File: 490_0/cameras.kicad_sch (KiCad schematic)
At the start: 2 parts, among them J1 ArduCAM ToF Camera, J2 ArduCAM ToF Camera

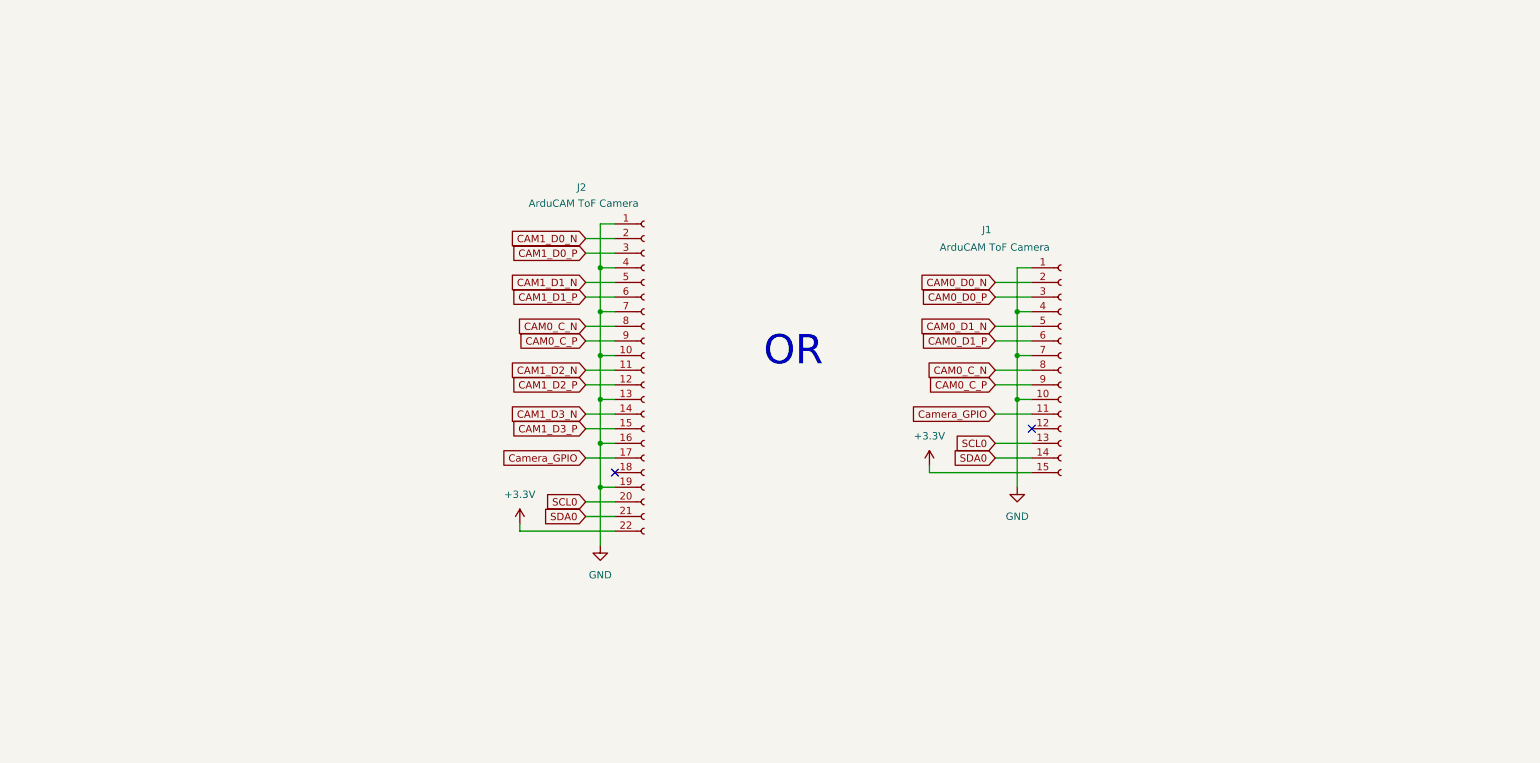
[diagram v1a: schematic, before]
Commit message: Changed the camera connectors
- Added 2 and 4 lane MIPI 22 lane connectors
- Added digikey link to a good type
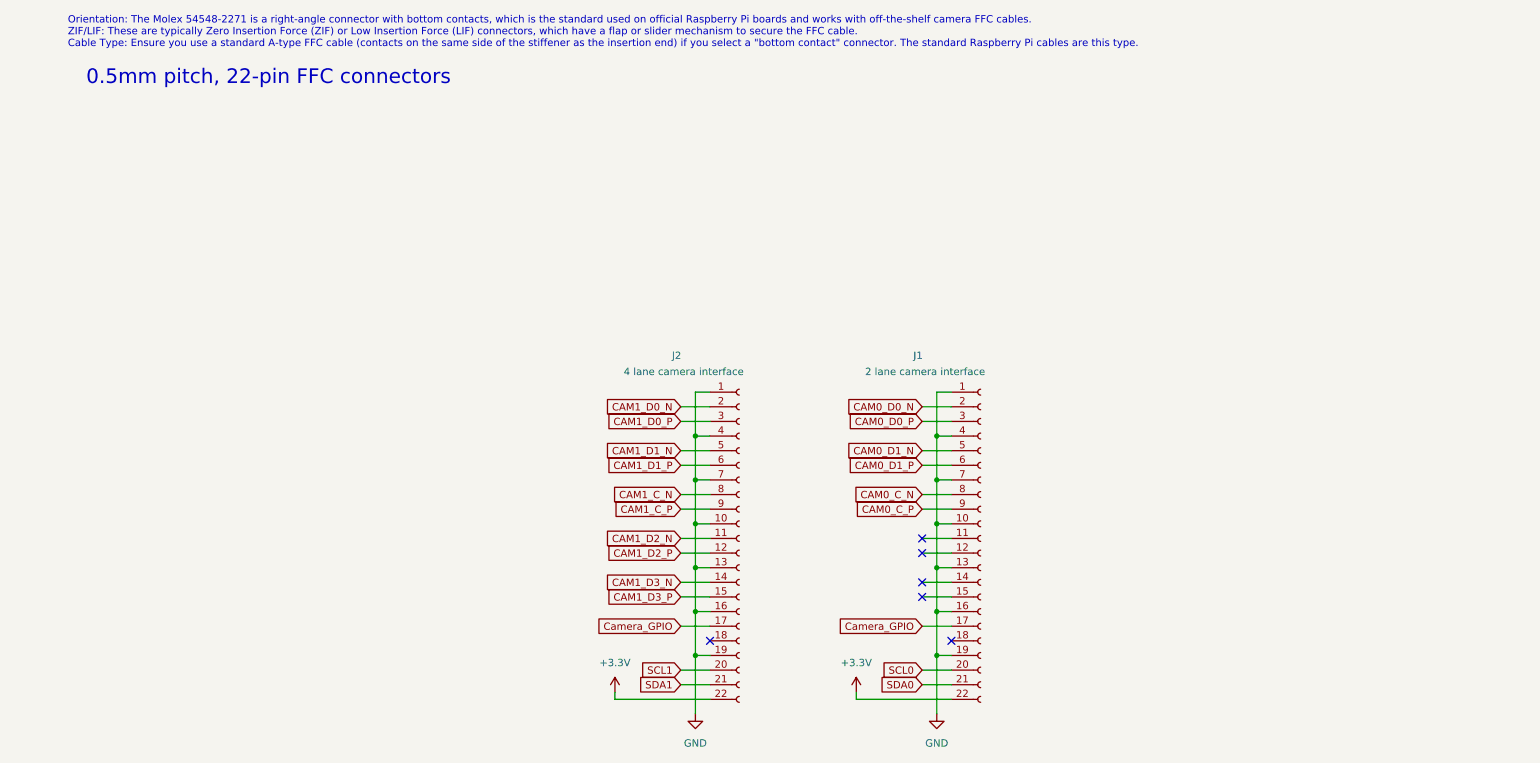
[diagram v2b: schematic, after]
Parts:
- removed J1: ArduCAM ToF Camera, symbol Connector:Conn_01x15_Socket
- added J1: 2 lane camera interface, symbol Connector:Conn_01x22_Socket
- J2: value ArduCAM ToF Camera -> 4 lane camera interface
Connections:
- net +3.3V: now also J1.22 (Pin_22)
- net CAM0_C_N: now also J1.8 (Pin_8); no longer J2.8 (Pin_8)
- net CAM0_C_P: now also J1.9 (Pin_9); no longer J2.9 (Pin_9)
- net CAM0_D0_N: now also J1.2 (Pin_2)
- net CAM0_D0_P: now also J1.3 (Pin_3)
- net CAM0_D1_N: now also J1.5 (Pin_5)
- net CAM0_D1_P: now also J1.6 (Pin_6)
- net Camera_GPIO: now also J1.17 (Pin_17)
- net GND: now also J1.1 (Pin_1), J1.10 (Pin_10), J1.13 (Pin_13), J1.16 (Pin_16), J1.19 (Pin_19), J1.4 (Pin_4), J1.7 (Pin_7)
- net SCL0: now also J1.20 (Pin_20); no longer J2.20 (Pin_20)
- net SDA0: now also J1.21 (Pin_21); no longer J2.21 (Pin_21)
- new net CAM1_C_N: J2.8 (Pin_8)
- new net CAM1_C_P: J2.9 (Pin_9)
- new net SCL1: J2.20 (Pin_20)
- new net SDA1: J2.21 (Pin_21)
- no-connect marks 2 -> 6
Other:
- note added: "0.5mm pitch, 22-pin FFC connectors"
- note added: "Orientation: The Molex 54548-2271 is a right-angle connector with bottom contacts, which is the standard used on official Raspberry Pi boards and works with off-the-shelf camera FFC cables. ZIF/LIF: These are typically Zero Insertion Force (ZIF) or Low Insertion Force (LIF) connectors, which have a flap or slider mechanism to secure the FFC cable. Cable Type: Ensure you use a standard A-type FFC 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"
- note removed: "OR"
- moved on the sheet: J2
